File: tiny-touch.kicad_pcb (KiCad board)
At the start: 2 copper layers, 100.3 x 67 mm, 122 parts, among them IC1 STM32F072VBT6, Q1 DTC123J, SW1 SW_Push, U1 MCP1700-3002E_SOT23, U2 SRV05-4

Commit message: Update
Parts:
- removed the REF** at (114.4, 75.0)
- removed the REF** at (209.7, 75.0)
- added REF**: MountingHole_2.2mm_M2, MountingHole:MountingHole_2.2mm_M2, F.Cu at (114.4, 66.0)
- added REF**: MountingHole_2.2mm_M2, MountingHole:MountingHole_2.2mm_M2, F.Cu at (209.7, 66.0)
- moved H1 88.9 mm to (201.3, 71.6), turned to 180 degrees
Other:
- board size 100.3 x 67 mm -> 100.3 x 76 mm
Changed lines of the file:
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@@
   )
   (module MountingHole:MountingHole_2.2mm_M2 (layer F.Cu)
-    (at 114.4 75)
+    (at 114.4 66)
     (descr "Mounting Hole 2.2mm, no annular, M2")
     (tags "mounting hole 2.2mm no annular m2")
@@
   )
   (module MountingHole:MountingHole_2.2mm_M2 (layer F.Cu)
-    (at 209.7 75)
+    (at 209.7 66)
     (descr "Mounting Hole 2.2mm, no annular, M2")
     (tags "mounting hole 2.2mm no annular m2")
@@
   )
   (module ckeys:microbit-clamp-hole-pad (layer F.Cu)
-    (at 264.011 134.59)
+    (at 201.3 71.6 180)
     (fp_text reference H1 (at 0 0.125) (layer F.Fab)
       (effects (font (size 0.1 0.1) (thickness 0.01)))
@@
       (effects (font (size 0.1 0.1) (thickness 0.01)))
     )
-    (fp_text user %R (at 0 0 -180) (layer Eco1.User)
+    (fp_text user %R (at 0 0 180) (layer Eco1.User)
       (effects (font (size 0.3 0.3) (thickness 0.03)))
     )
@@
     (fp_line (start -2.7 8.2) (end 2.7 8.2) (layer F.CrtYd) (width 0.05))
     (fp_line (start -2.7 0) (end -2.7 8.2) (layer F.CrtYd) (width 0.05))
-    (pad 1 thru_hole circle (at 0 0) (size 5 5) (drill 4) (layers *.Cu *.Mask)
+    (pad 1 thru_hole circle (at 0 0 180) (size 5 5) (drill 4) (layers *.Cu *.Mask)
       (net 7 "Net-(H1-Pad1)"))
-    (pad 1 smd rect (at 0 4) (size 5 8) (layers F.Cu F.Mask)
+    (pad 1 smd rect (at 0 4 180) (size 5 8) (layers F.Cu F.Mask)
       (net 7 "Net-(H1-Pad1)"))
-    (pad 1 smd rect (at 0 4) (size 5 8) (layers *.Mask B.Cu)
+    (pad 1 smd rect (at 0 4 180) (size 5 8) (layers *.Mask B.Cu)
       (net 7 "Net-(H1-Pad1)"))
   )
@@
   )
   (gr_line (start 113.9 139.5) (end 210.2 139.5) (layer Edge.Cuts) (width 0.05))
-  (gr_line (start 111.9 74.5) (end 111.9 137.5) (layer Edge.Cuts) (width 0.05))
-  (gr_line (start 210.2 72.5) (end 113.9 72.5) (layer Edge.Cuts) (width 0.05))
-  (gr_line (start 212.2 137.5) (end 212.2 74.5) (layer Edge.Cuts) (width 0.05))
+  (gr_line (start 111.9 65.5) (end 111.9 137.5) (layer Edge.Cuts) (width 0.05))
+  (gr_line (start 210.2 63.5) (end 113.9 63.5) (layer Edge.Cuts) (width 0.05))
+  (gr_line (start 212.2 137.5) (end 212.2 65.5) (layer Edge.Cuts) (width 0.05))
   (gr_arc (start 113.9 137.5) (end 111.9 137.5) (angle -90) (layer Edge.Cuts) (width 0.05))
-  (gr_arc (start 113.9 74.5) (end 113.9 72.5) (angle -90) (layer Edge.Cuts) (width 0.05))
-  (gr_arc (start 210.2 74.5) (end 212.2 74.5) (angle -90) (layer Edge.Cuts) (width 0.05))
+  (gr_arc (start 113.9 65.5) (end 113.9 63.5) (angle -90) (layer Edge.Cuts) (width 0.05))
+  (gr_arc (start 210.2 65.5) (end 212.2 65.5) (angle -90) (layer Edge.Cuts) (width 0.05))
   (gr_arc (start 210.2 137.5) (end 210.2 139.5) (angle -90) (layer Edge.Cuts) (width 0.05))
 )

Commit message: Start running traces
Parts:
- C1, C10, C11, C2, C3, C4, C5, C6, C7, C8, C9, D1, D2, IC1, PF1, Q1, R1, R2, R3, R4, R5, R6, SW1, U1, U2, USB1: moved to B.Cu
- moved C11 185.3 mm to (127.4, 78.5)
- moved C9 180.9 mm to (136.1, 78.5)
- moved C3 179.3 mm to (138.3, 73.7)
- moved C6 177.5 mm to (125.1, 73.7)
- moved C10 173.5 mm to (131.7, 78.5)
- moved C5 172.6 mm to (129.4, 73.7)
- moved C1 171.9 mm to (147.5, 73.7)
- moved C7 168.3 mm to (144.9, 78.5)
- moved C2 168.2 mm to (142.9, 73.7)
- moved C8 164.5 mm to (140.5, 78.5)
- moved C4 160.4 mm to (133.8, 73.7)
- moved U2 154.1 mm to (158.9, 78.6)
- moved PF1 142.6 mm to (151.6, 78.5)
- moved R5 141.2 mm to (175.4, 72.6)
- moved R6 140.6 mm to (170.8, 72.6)
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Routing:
- net +3V3: track 0.00 -> 184.8 mm, vias 0 -> 6
- net NRST: track 0.00 -> 68.1 mm
- net BOOTO: track 0.00 -> 67.3 mm
- net E2: track 0.00 -> 64.7 mm, vias 0 -> 1
- net C13: track 0.00 -> 55.2 mm, vias 0 -> 1
- net E5: track 0.00 -> 52.5 mm, vias 0 -> 1
- net E3: track 0.00 -> 50.9 mm, vias 0 -> 1
- net E4: track 0.00 -> 49.7 mm, vias 0 -> 1
- net Net-(D2-Pad2): track 0.00 -> 44.0 mm
- net F10: track 0.00 -> 43.2 mm, vias 0 -> 1
- net C14: track 0.00 -> 42.3 mm, vias 0 -> 1
- net F0: track 0.00 -> 41.5 mm, vias 0 -> 1
- net GNDREF: track 0.00 -> 38.8 mm
- net E6: track 0.00 -> 37.5 mm, vias 0 -> 1
- net F9: track 0.00 -> 33.9 mm, vias 0 -> 1
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- added copper zone on B.Cu, net GND
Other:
- net class PWR added: clearance 0.2, trace_width 0.25, via_dia 0.8, via_drill 0.4

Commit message: Continue tracing
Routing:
- net A2: track 0.00 -> 118.3 mm, vias 0 -> 5
- net A1: track 0.00 -> 113.1 mm, vias 0 -> 3
- net F3: track 0.00 -> 112.0 mm, vias 0 -> 3
- net A0: track 0.00 -> 104.6 mm, vias 0 -> 5
- net C1: track 0.00 -> 86.5 mm, vias 0 -> 1
- net F2: track 0.00 -> 76.3 mm, vias 0 -> 1
- net F1: track 0.00 -> 59.5 mm, vias 0 -> 1
- net NRST: track 68.1 -> 127.0 mm
- net C0: track 0.00 -> 53.8 mm, vias 0 -> 1
- net C2: track 0.00 -> 46.6 mm, vias 0 -> 3
- net A3: track 0.00 -> 35.6 mm, vias 0 -> 1
- net C3: track 0.00 -> 33.3 mm, vias 0 -> 3
- net A4: track 0.00 -> 32.9 mm, vias 0 -> 1
- net C4: track 0.00 -> 29.4 mm, vias 0 -> 1
- net BOOTO: track 67.3 -> 86.1 mm
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
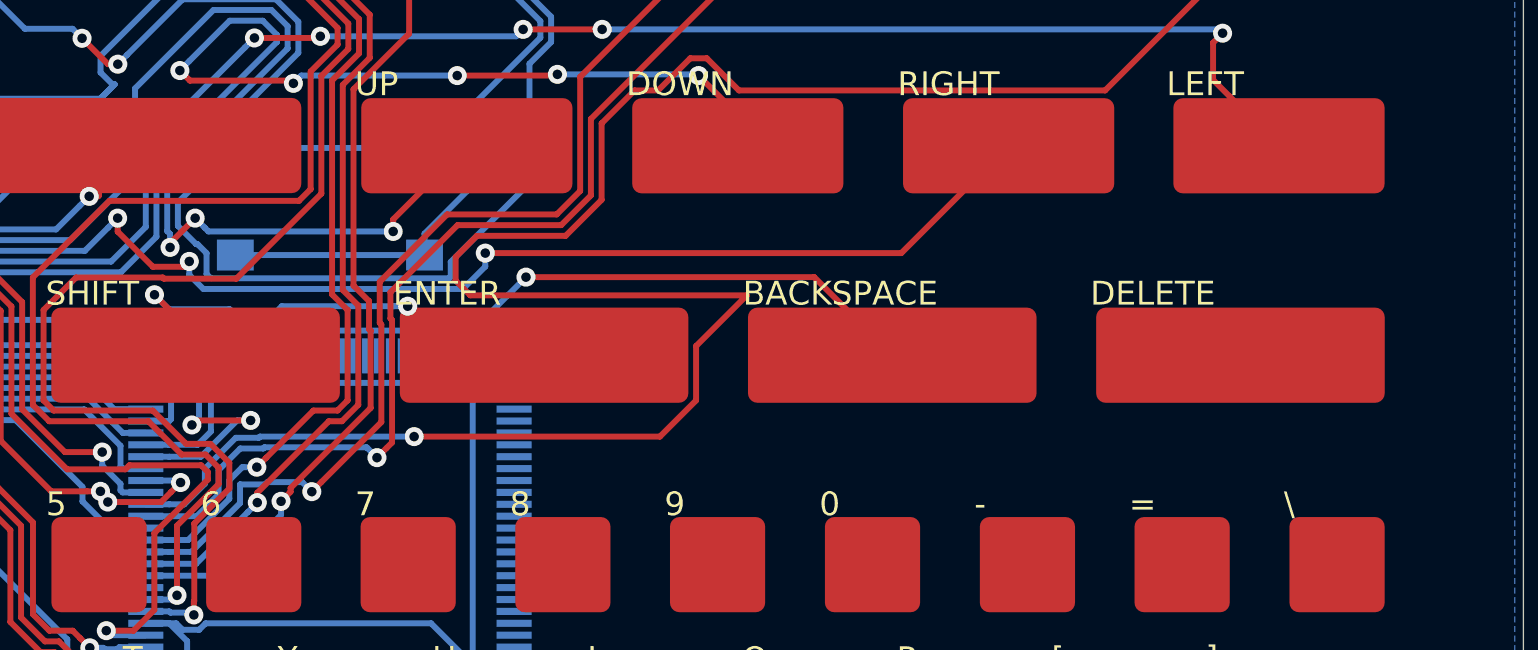
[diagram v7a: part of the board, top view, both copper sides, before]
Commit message: Try to add more traces
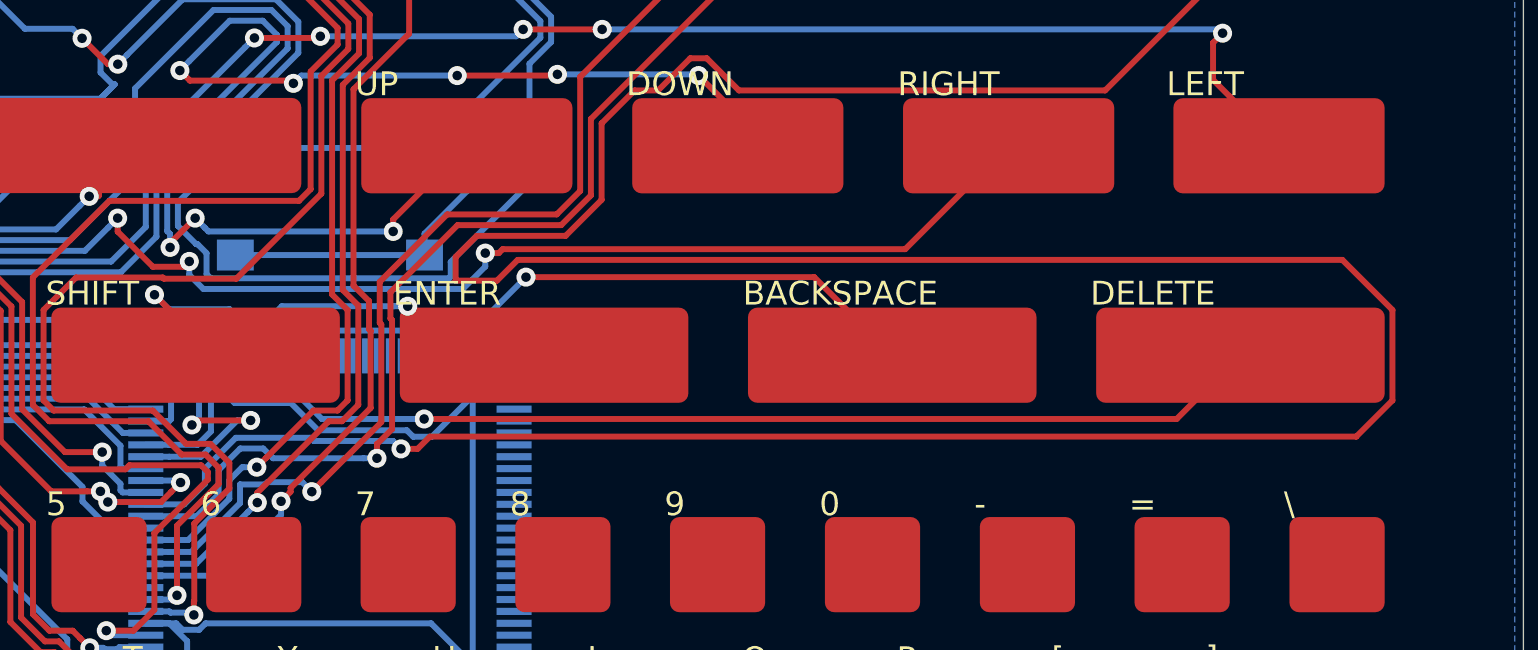
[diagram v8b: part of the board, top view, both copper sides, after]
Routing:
- net C1: track 86.5 -> 142.7 mm
- net C5: track 0.00 -> 43.0 mm, vias 0 -> 1
- net +3V3: track 196.9 -> 199.2 mm
